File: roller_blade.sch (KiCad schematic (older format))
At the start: 1 part

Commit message: Added microcontroller sheet
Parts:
- removed U?: ATMEGA328PB-AU, Housings_QFP:TQFP-32_7x7mm_Pitch0.8mm, symbol ATMEGA328PB-AU
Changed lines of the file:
@@
 LIBS:contrib
 LIBS:valves
+LIBS:testpart
+LIBS:roller_blade-cache
 EELAYER 25 0
 EELAYER END
 $Descr A4 11693 8268
 encoding utf-8
-Sheet 1 1
+Sheet 1 6
 Title ""
 Date ""
@@
 Comment4 ""
 $EndDescr
-$Comp
-L ATMEGA328PB-AU U?
-U 1 1 5A87136C
-P 2350 2400
-F 0 "U?" H 1950 3875 50  0000 R BNN
-F 1 "ATMEGA328PB-AU" H 1950 3800 50  0000 R BNN
-F 2 "Housings_QFP:TQFP-32_7x7mm_Pitch0.8mm" H 2300 1000 50  0001 L CIN
-F 3 "" H 2050 2450 50  0001 C CNN
-	1    2350 2400
-	1    0    0    -1
-$EndComp
+$Sheet
+S 5000 4650 2100 1450
+U 5A997994
+F0 "MCU" 59
+F1 "MCU.sch" 59
+$EndSheet
+$Sheet
+S 7850 2650 1600 800
+U 5A9979B5
+F0 "reciever_mod" 59
+F1 "reciever_mod.sch" 59
+$EndSheet
+$Sheet
+S 5550 2050 1100 650
+U 5A9979FE
+F0 "FS" 59
+F1 "FS.sch" 59
+$EndSheet
+$Sheet
+S 4400 3150 650  300
+U 5A997A12
+F0 "encoder" 59
+F1 "encoder.sch" 59
+$EndSheet
+$Sheet
+S 2350 5200 700  700
+U 5A997A29
+F0 "power" 59
+F1 "power.sch" 59
+$EndSheet
 $EndSCHEMATC

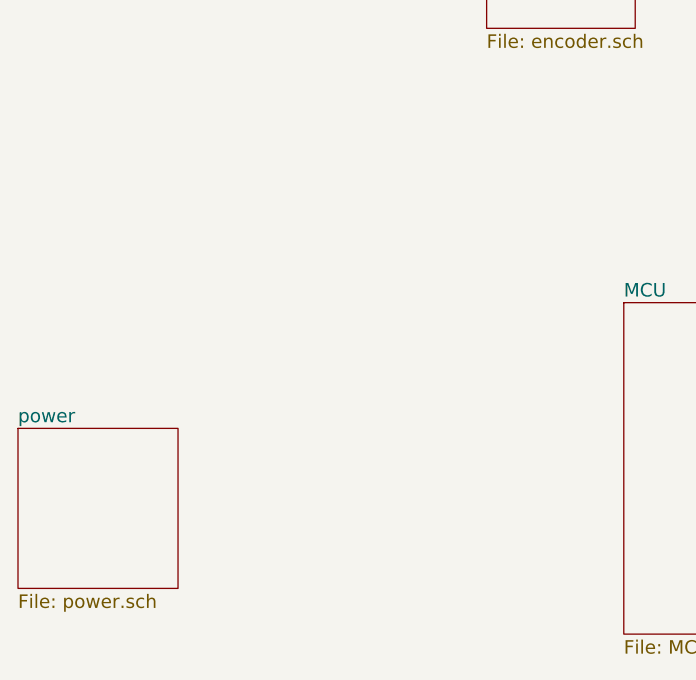
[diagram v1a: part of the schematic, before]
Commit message: Did power and encoder
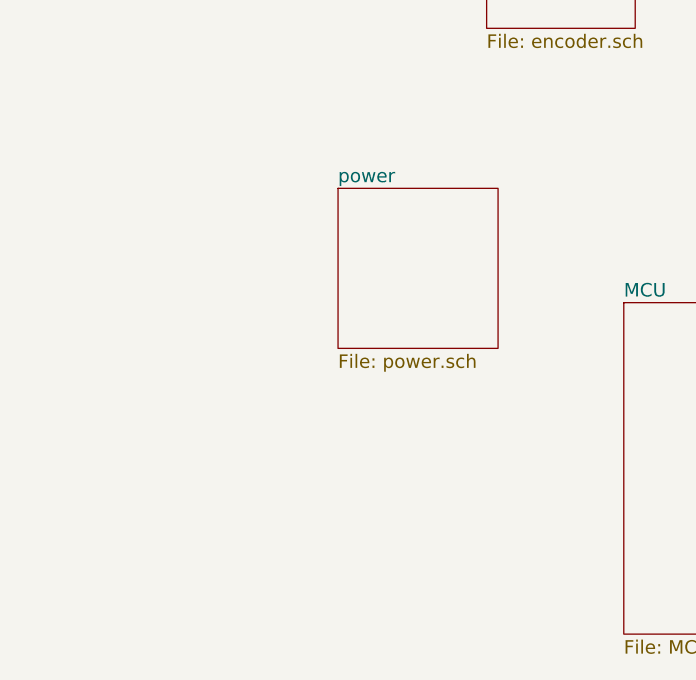
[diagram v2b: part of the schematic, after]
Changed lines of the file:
@@
 LIBS:contrib
 LIBS:valves
-LIBS:testpart
+LIBS:CustomComponents
 LIBS:roller_blade-cache
 EELAYER 25 0
@@
 $EndSheet
 $Sheet
-S 2350 5200 700  700
+S 3750 4150 700  700
 U 5A997A29
 F0 "power" 59
